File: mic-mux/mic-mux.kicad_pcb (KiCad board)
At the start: 4 copper layers, 142.2 x 214 mm, 325 parts, among them J1 MIC-IN, J10 I2C and Reset (Top-Male), J11 Power Out (Top-Male), J12 Extra GPIO, J2 MIC-OUT, J3 Headphone MUX Audio IN (Top-M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, J4 Headphone MUX Audio OUT (Top-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, J5 I2C and Reset, J6 Power In, J7 Headphone MUX Audio IN (Botto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, J8 Headphone MUX Audio OUT (Bott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, J9 GND, U1 ADG715, U10 TCA9555, U11 TCA9555, U12 OPA1604, U13 DS1882, U14 OPA1604, U15 DS1882, U16 OPA1604, U17 DS1882, U18 OPA1604, U19 DS1882, U2 ADG708, U20 OPA1604, U21 OPA1602, U22 OPA1604, U23 OPA1604, U24 OPA1604, U25 OPA1604, U26 OPA1602, U27 OPA1604, U28 OPA1604, U29 OPA1604, U3 ADG708, U30 OPA1604, U31 OPA1602, U32 OPA1604, U33 OPA1604, U34 OPA1604, U35 OPA1604, U36 OPA1602, U37 OPA1604, U38 OPA1604, U39 OPA1604, U4 ADG708, U5 ADG708, U6 ADG708, U7 ADG708, U8 ADG708, U9 ADG708

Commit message: Finished mic mux
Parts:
- J1, J9: moved to B.Cu
- moved J1 81.7 mm to (127.0, 269.2)
- moved C26 33.5 mm to (67.3, 189.2), turned to 270 degrees
- moved C25 33.3 mm to (65.2, 189.2), turned to 270 degrees
- moved C23 30.8 mm to (69.5, 189.2)
- moved C24 30.8 mm to (71.6, 189.2)
- moved R17 30.2 mm to (82.0, 231.4), turned to 180 degrees
- moved C29 30.0 mm to (79.8, 228.6), turned to 270 degrees
- moved R16 28.0 mm to (77.7, 228.6), turned to 90 degrees
- moved C45 27.4 mm to (174.2, 228.6), turned to 270 degrees
- moved C21 26.9 mm to (79.8, 188.0), turned to 270 degrees
- moved R8 26.9 mm to (77.7, 188.0), turned to 90 degrees
- moved R32 26.9 mm to (172.2, 228.6), turned to 90 degrees
- moved R13 25.8 mm to (82.0, 241.0), turned to 180 degrees
- moved R14 25.1 mm to (77.5, 231.4), turned to 0 degrees
- moved C37 24.7 mm to (174.2, 188.0), turned to 270 degrees
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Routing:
- net +5V: track 21.2 -> 410.0 mm, vias 4 -> 6
- net +5VA: track 28.7 -> 360.7 mm, vias 4 -> 5
- net -5VA: track 22.1 -> 333.3 mm, vias 4 -> 5
- net /5V-SDA-1: track 20.6 -> 281.4 mm, vias 0 -> 6
- net /5V-SCL-1: track 21.2 -> 279.1 mm, vias 0 -> 4
- net /2v5-SCL-0: track 152.1 -> 326.8 mm
- net /SPST-~RST: track 96.3 -> 268.5 mm
- net -2.5V: track 128.5 -> 295.5 mm, vias 9 -> 10
- net +2V5: track 235.4 -> 400.2 mm
- net /2v5-SDA-0: track 142.5 -> 307.1 mm
- net /MIC-IN5: track 0.00 -> 157.8 mm
- net /MIC-IN1: track 0.00 -> 153.3 mm
- net -12VA: track 174.7 -> 305.5 mm
- net /MIC-IN0: track 0.00 -> 126.8 mm
- net +12VA: track 85.8 -> 212.4 mm
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- added copper zone on In1.Cu, net +12VA
- removed copper zone on In1.Cu, net +12V
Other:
- board size 142.2 x 214 mm -> 142.2 x 203.8 mm
- board text added: "Use 25 mil grid for PCB outline Use 25 mil grid for zones"
- board text removed: "Use 50 mil grid for PCB outline Use 5 mil grid for zones"

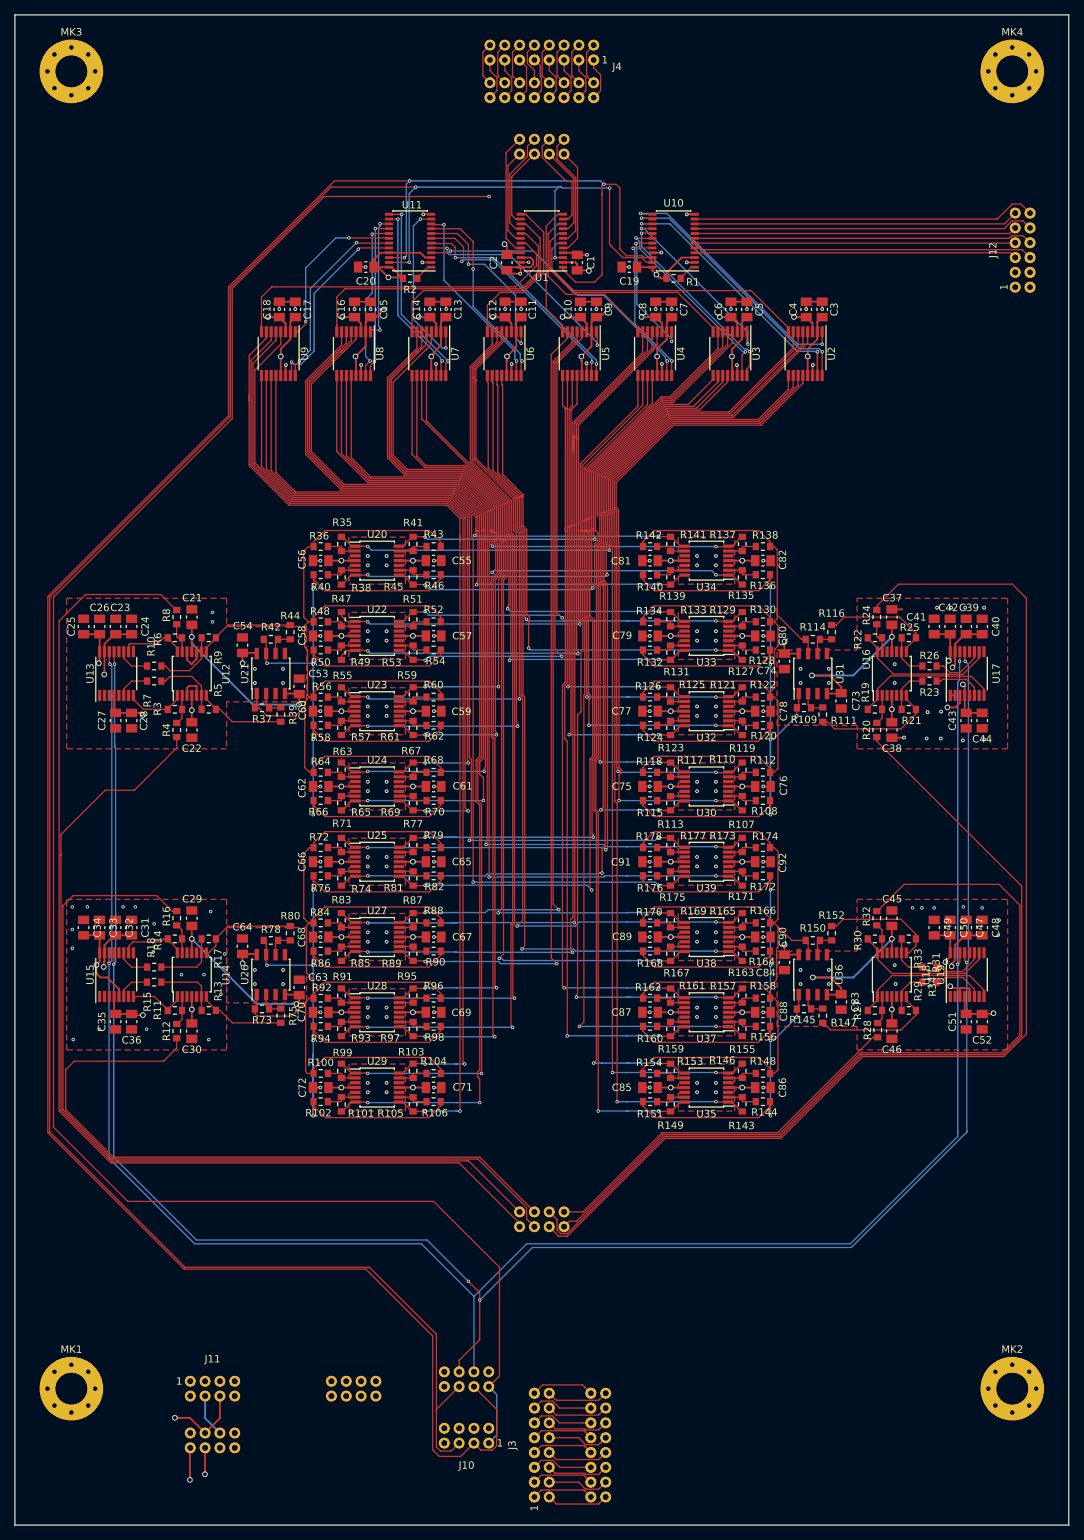
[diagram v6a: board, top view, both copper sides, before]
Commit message: Minor updates and aligning tracks
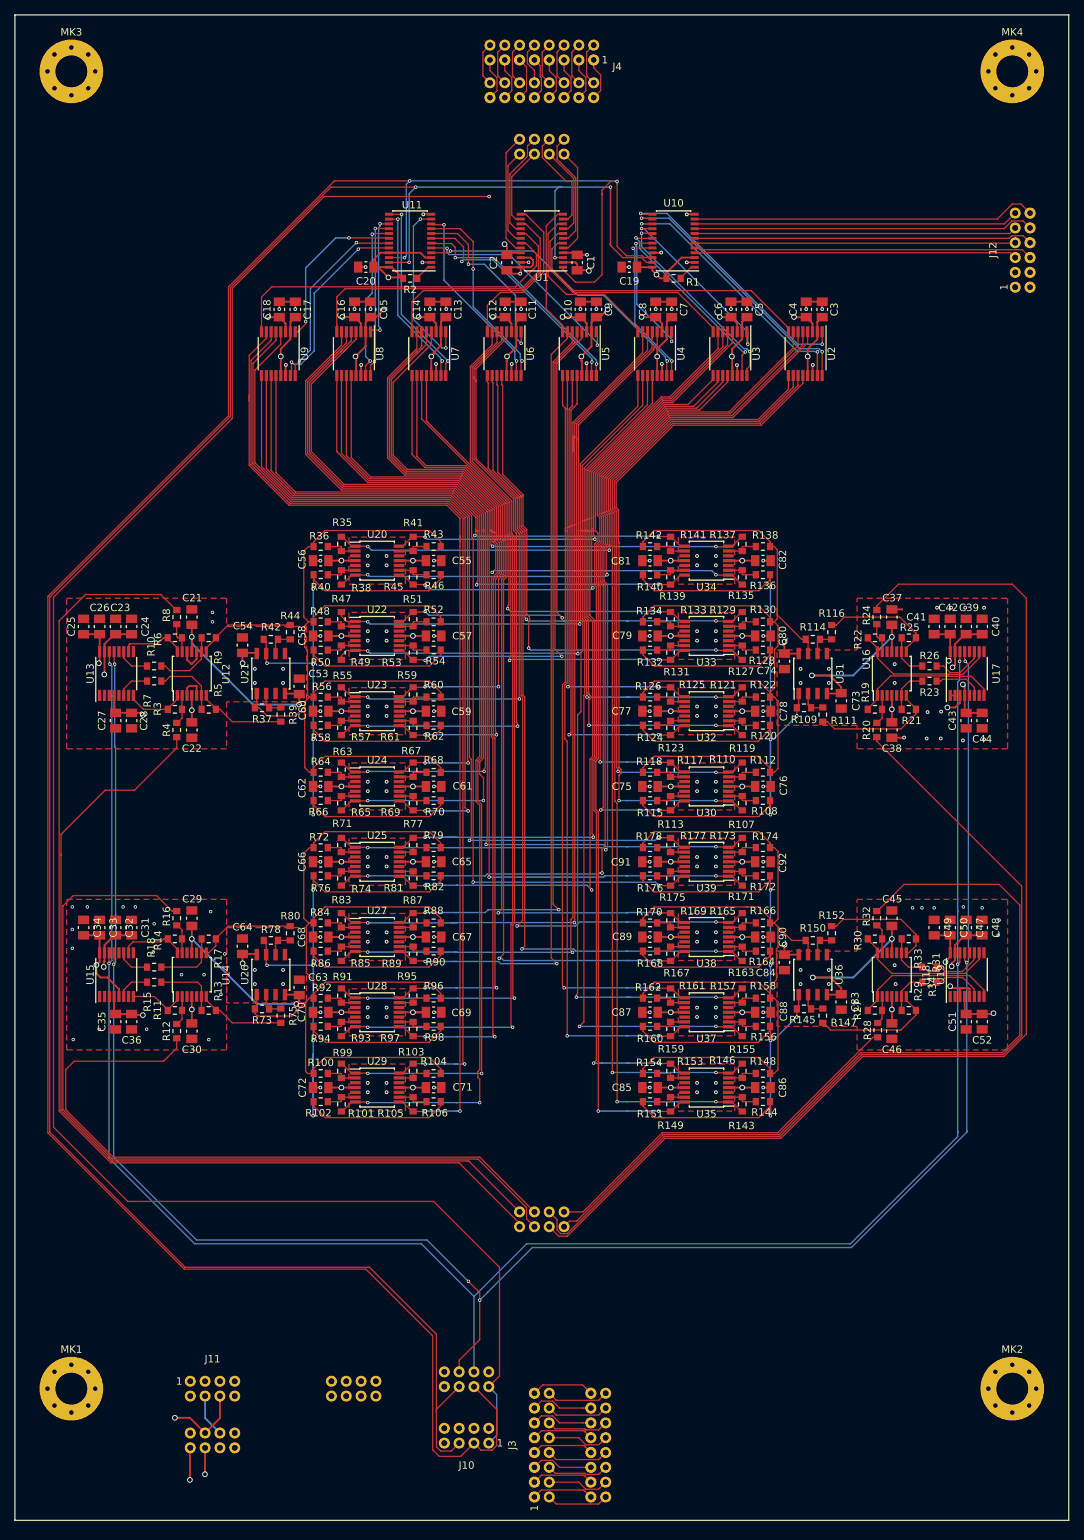
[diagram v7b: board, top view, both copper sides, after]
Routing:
- net /2v5-SDA-0: track 307.1 -> 314.6 mm
- net /2v5-SCL-0: track 326.8 -> 328.7 mm
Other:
- board size 142.2 x 203.8 mm -> 142.2 x 203.2 mm
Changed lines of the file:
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@@
   (general
     (thickness 1.6)
-    (drawings 43)
-    (tracks 3962)
+    (drawings 45)
+    (tracks 3963)
     (zones 0)
     (modules 325)
@@
     )
   )
+  (dimension 142.24 (width 0.3) (layer Dwgs.User)
+    (gr_text "5.6000 in" (at 127 89.455) (layer Dwgs.User)
+      (effects (font (size 1.5 1.5) (thickness 0.3)))
+    )
+    (feature1 (pts (xy 55.88 106.68) (xy 55.88 88.105)))
+    (feature2 (pts (xy 198.12 106.68) (xy 198.12 88.105)))
+    (crossbar (pts (xy 198.12 90.805) (xy 55.88 90.805)))
+    (arrow1a (pts (xy 55.88 90.805) (xy 57.006504 90.218579)))
+    (arrow1b (pts (xy 55.88 90.805) (xy 57.006504 91.391421)))
+    (arrow2a (pts (xy 198.12 90.805) (xy 196.993496 90.218579)))
+    (arrow2b (pts (xy 198.12 90.805) (xy 196.993496 91.391421)))
+  )
+  (dimension 203.2 (width 0.3) (layer Dwgs.User)
+    (gr_text "8.0000 in" (at 208.36 208.28 270) (layer Dwgs.User)
+      (effects (font (size 1.5 1.5) (thickness 0.3)))
+    )
+    (feature1 (pts (xy 198.12 309.88) (xy 209.71 309.88)))
+    (feature2 (pts (xy 198.12 106.68) (xy 209.71 106.68)))
+    (crossbar (pts (xy 207.01 106.68) (xy 207.01 309.88)))
+    (arrow1a (pts (xy 207.01 309.88) (xy 206.423579 308.753496)))
+    (arrow1b (pts (xy 207.01 309.88) (xy 207.596421 308.753496)))
+    (arrow2a (pts (xy 207.01 106.68) (xy 206.423579 107.806504)))
+    (arrow2b (pts (xy 207.01 106.68) (xy 207.596421 107.806504)))
+  )
   (dimension 22.86 (width 0.3) (layer Dwgs.User)
     (gr_text "0.9000 in" (at 29.765 280.67 270) (layer Dwgs.User)
@@
   (gr_line (start 127 124.46) (end 127 285.75) (layer Eco1.User) (width 0.0254))
   (gr_line (start 157.861 170.815) (end 157.861 170.815) (layer Eco1.User) (width 0.0254))
-  (gr_line (start 55.88 310.515) (end 198.12 310.515) (layer Edge.Cuts) (width 0.0254))
+  (gr_line (start 55.88 309.88) (end 198.12 309.88) (layer Edge.Cuts) (width 0.0254))
   (gr_line (start 55.88 317.5) (end 55.88 317.5) (layer Edge.Cuts) (width 0.0254))
-  (gr_line (start 55.88 106.68) (end 55.88 310.515) (layer Edge.Cuts) (width 0.0254))
+  (gr_line (start 55.88 106.68) (end 55.88 309.88) (layer Edge.Cuts) (width 0.0254))
   (gr_line (start 198.12 325.12) (end 198.12 325.12) (layer Edge.Cuts) (width 0.0254))
-  (gr_line (start 198.12 106.68) (end 198.12 310.515) (layer Edge.Cuts) (width 0.0254))
+  (gr_line (start 198.12 106.68) (end 198.12 309.88) (layer Edge.Cuts) (width 0.0254))
   (gr_line (start 55.88 106.68) (end 198.12 106.68) (layer Edge.Cuts) (width 0.0254))
   (gr_line (start 113.157 256.667) (end 113.157 256.667) (layer Eco1.User) (width 0.0254))
@@
   (segment (start 134.667499 293.672501) (end 134.870001 293.469999) (width 0.127) (layer F.Cu) (net 72))
   (segment (start 134.870001 293.469999) (end 135.62 292.72) (width 0.127) (layer F.Cu) (net 72))
+  (segment (start 135.128 130.31673) (end 136.28573 129.159) (width 0.127) (layer F.Cu) (net 89))
+  (segment (start 135.128 130.937) (end 135.128 130.31673) (width 0.127) (layer F.Cu) (net 89))
+  (segment (start 136.836711 129.159) (end 137.16 129.159) (width 0.127) (layer F.Cu) (net 89))
+  (segment (start 136.28573 129.159) (end 136.836711 129.159) (width 0.127) (layer F.Cu) (net 89))
+  (segment (start 109.169211 129.082789) (end 137.083789 129.082789) (width 0.127) (layer B.Cu) (net 89))
+  (segment (start 137.16 129.482289) (end 137.16 129.159) (width 0.127) (layer F.Cu) (net 89))
+  (segment (start 141.93 139.435) (end 140.825727 139.435) (width 0.127) (layer F.Cu) (net 89))
+  (segment (start 137.16 137.922) (end 137.16 129.482289) (width 0.127) (layer F.Cu) (net 89))
+  (segment (start 140.582716 139.191989) (end 138.429989 139.191989) (width 0.127) (layer F.Cu) (net 89))
+  (segment (start 137.083789 129.082789) (end 137.16 129.159) (width 0.127) (layer B.Cu) (net 89))
+  (segment (start 140.825727 139.435) (end 140.582716 139.191989) (width 0.127) (layer F.Cu) (net 89))
+  (segment (start 138.429989 139.191989) (end 137.16 137.922) (width 0.127) (layer F.Cu) (net 89))
+  (via (at 137.16 129.159) (size 0.4572) (drill 0.254) (layers F.Cu B.Cu) (net 89))
   (segment (start 112.268 300.355) (end 113.157 301.244) (width 0.127) (layer F.Cu) (net 89))
   (segment (start 113.157 301.244) (end 116.046 301.244) (width 0.127) (layer F.Cu) (net 89))
@@
   (segment (start 120.907501 294.897501) (end 118.589999 292.579999) (width 0.127) (layer F.Cu) (net 89))
   (segment (start 118.589999 292.579999) (end 117.84 291.83) (width 0.127) (layer F.Cu) (net 89))
-  (segment (start 137.033 129.54) (end 135.382 129.54) (width 0.127) (layer F.Cu) (net 89))
-  (via (at 135.382 129.54) (size 0.4572) (drill 0.254) (layers F.Cu B.Cu) (net 89))
   (segment (start 109.169211 129.082789) (end 108.712 129.54) (width 0.127) (layer B.Cu) (net 89))
   (segment (start 108.712 129.54) (end 108.712 139.192) (width 0.127) (layer B.Cu) (net 89))
@@
   (segment (start 108.447 139.435) (end 108.458 139.446) (width 0.127) (layer F.Cu) (net 89))
   (segment (start 106.37 139.435) (end 108.447 139.435) (width 0.127) (layer F.Cu) (net 89) (status 10))
-  (segment (start 134.924789 129.082789) (end 109.169211 129.082789) (width 0.127) (layer B.Cu) (net 89))
-  (segment (start 135.382 129.54) (end 134.924789 129.082789) (width 0.127) (layer B.Cu) (net 89))
-  (segment (start 135.382 129.54) (end 135.255 129.54) (width 0.127) (layer F.Cu) (net 89))
   (segment (start 135.128 141.732) (end 135.128 130.937) (width 0.127) (layer F.Cu) (net 89))
-  (segment (start 137.541 130.048) (end 137.033 129.54) (width 0.127) (layer F.Cu) (net 89))
   (segment (start 135.128 130.937) (end 135.128 130.81) (width 0.127) (layer F.Cu) (net 89))
-  (segment (start 135.128 129.667) (end 135.128 130.937) (width 0.127) (layer F.Cu) (net 89))
-  (segment (start 141.93 139.435) (end 140.825727 139.435) (width 0.127) (layer F.Cu) (net 89) (status 10))
-  (segment (start 135.255 129.54) (end 135.128 129.667) (width 0.127) (layer F.Cu) (net 89))
-  (segment (start 140.825727 139.435) (end 140.582716 139.191989) (width 0.127) (layer F.Cu) (net 89))
-  (segment (start 140.582716 139.191989) (end 138.429989 139.191989) (width 0.127) (layer F.Cu) (net 89))
-  (segment (start 138.429989 139.191989) (end 137.541 138.303) (width 0.127) (layer F.Cu) (net 89))
-  (segment (start 137.541 138.303) (end 137.541 130.048) (width 0.127) (layer F.Cu) (net 89))
   (segment (start 134.112 142.748) (end 135.128 141.732) (width 0.127) (layer F.Cu) (net 89))
   (segment (start 131.536 142.748) (end 134.112 142.748) (width 0.127) (layer F.Cu) (net 89))
   (segment (start 129.85 140.735) (end 129.85 141.062) (width 0.127) (layer F.Cu) (net 89) (status 10))
   (segment (start 129.85 141.062) (end 131.536 142.748) (width 0.127) (layer F.Cu) (net 89))
+  (segment (start 136.271 130.244289) (end 136.271 129.921) (width 0.127) (layer F.Cu) (net 90))
+  (segment (start 129.667 129.921) (end 136.271 129.921) (width 0.127) (layer B.Cu) (net 90))
+  (segment (start 136.398 137.922) (end 136.271 137.795) (width 0.127) (layer F.Cu) (net 90))
+  (segment (start 136.271 137.795) (end 136.271 130.244289) (width 0.127) (layer F.Cu) (net 90))
+  (segment (start 136.144 137.668) (end 136.271 137.541) (width 0.127) (layer F.Cu) (net 90))
+  (via (at 136.271 129.921) (size 0.4572) (drill 0.254) (layers F.Cu B.Cu) (net 90))
+  (segment (start 136.271 137.541) (end 136.271 130.244289) (width 0.127) (layer F.Cu) (net 90))
   (segment (start 60.579011 257.450787) (end 78.845213 275.716989) (width 0.127) (layer F.Cu) (net 90))
   (segment (start 98.530224 129.921) (end 84.963011 143.488213) (width 0.127) (layer F.Cu) (net 90))
@@
   (segment (start 112.772499 294.897501) (end 115.090001 292.579999) (width 0.127) (layer F.Cu) (net 90))
   (segment (start 115.090001 292.579999) (end 115.84 291.83) (width 0.127) (layer F.Cu) (net 90))
-  (segment (start 129.794 130.048) (end 136.144 130.048) (width 0.127) (layer B.Cu) (net 90))
-  (segment (start 129.667 129.921) (end 129.794 130.048) (width 0.127) (layer B.Cu) (net 90))
   (segment (start 129.667 129.921) (end 109.982 129.921) (width 0.127) (layer B.Cu) (net 90))
   (via (at 109.982 129.921) (size 0.4572) (drill 0.254) (layers F.Cu B.Cu) (net 90))
@@
   (segment (start 109.982 129.921) (end 109.093 130.81) (width 0.127) (layer B.Cu) (net 90))
   (segment (start 137.922 139.446) (end 136.398 137.922) (width 0.127) (layer F.Cu) (net 90))
-  (segment (start 136.398 137.922) (end 136.271 137.795) (width 0.127) (layer F.Cu) (net 90))
-  (segment (start 136.144 130.048) (end 136.144 137.668) (width 0.127) (layer F.Cu) (net 90))
-  (segment (start 136.144 137.668) (end 136.398 137.922) (width 0.127) (layer F.Cu) (net 90))
-  (via (at 136.144 130.048) (size 0.4572) (drill 0.254) (layers F.Cu B.Cu) (net 90))
   (segment (start 128.778 130.429) (end 129.286 129.921) (width 0.127) (layer B.Cu) (net 90))
   (segment (start 128.778 139.446) (end 128.778 130.429) (width 0.127) (layer B.Cu) (net 90))
@@
     (polygon
       (pts
-        (xy 55.88 106.68) (xy 198.12 106.68) (xy 198.12 310.515) (xy 55.88 310.515)
+        (xy 55.88 106.68) (xy 198.12 106.68) (xy 198.12 309.88) (xy 55.88 309.88)
       )
     )
     (polygon
       (pts
-        (xy 56.515 309.88) (xy 197.485 309.88) (xy 197.485 107.315) (xy 56.515 107.315)
+        (xy 56.515 309.245) (xy 197.485 309.245) (xy 197.485 107.315) (xy 56.515 107.315)
       )
     )
@@
     (polygon
       (pts
-        (xy 56.515 107.315) (xy 55.88 310.515) (xy 196.85 310.515) (xy 197.485 107.315)
+        (xy 56.515 107.315) (xy 56.515 309.245) (xy 197.485 309.245) (xy 197.485 107.315)
       )
     )
